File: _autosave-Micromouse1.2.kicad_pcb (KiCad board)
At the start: 2 copper layers, 70.4 x 87.9 mm, 117 parts, among them J1 USB_B, P1 CONN_01X4, Q1 Q_NMOS_DGS, Q2 Q_NMOS_DGS, Q3 Q_NMOS_DGS, Q4 Q_NMOS_DGS, Q5 Q_NMOS_DGS, Q6 Q_NMOS_DGS, U1 BAT54C, U10 CONN_02X03, U14 ferrite, U15 LMZ21701, U16 JST_Connector, U17 Switch_micromouse, U18 LMZ21701, U19 splitter, U2 DRV8833, U20 TPD3S014, U21 MKL02Z32VFG4, U22 LP38691, U23 MK66FX1M0, U24 Test_Point, U25 Test_Point, U26 Test_Point, U27 Test_Point, U28 Test_Point, U29 Test_Point, U3 ferrite, U30 Test_Point, U31 MPU-6500, U32 Motor_mount, U5 ferrite, U6 BAT54C, U9 CONN_02X03, Y1 Crystal_16MHz, Y2 32.768MHz

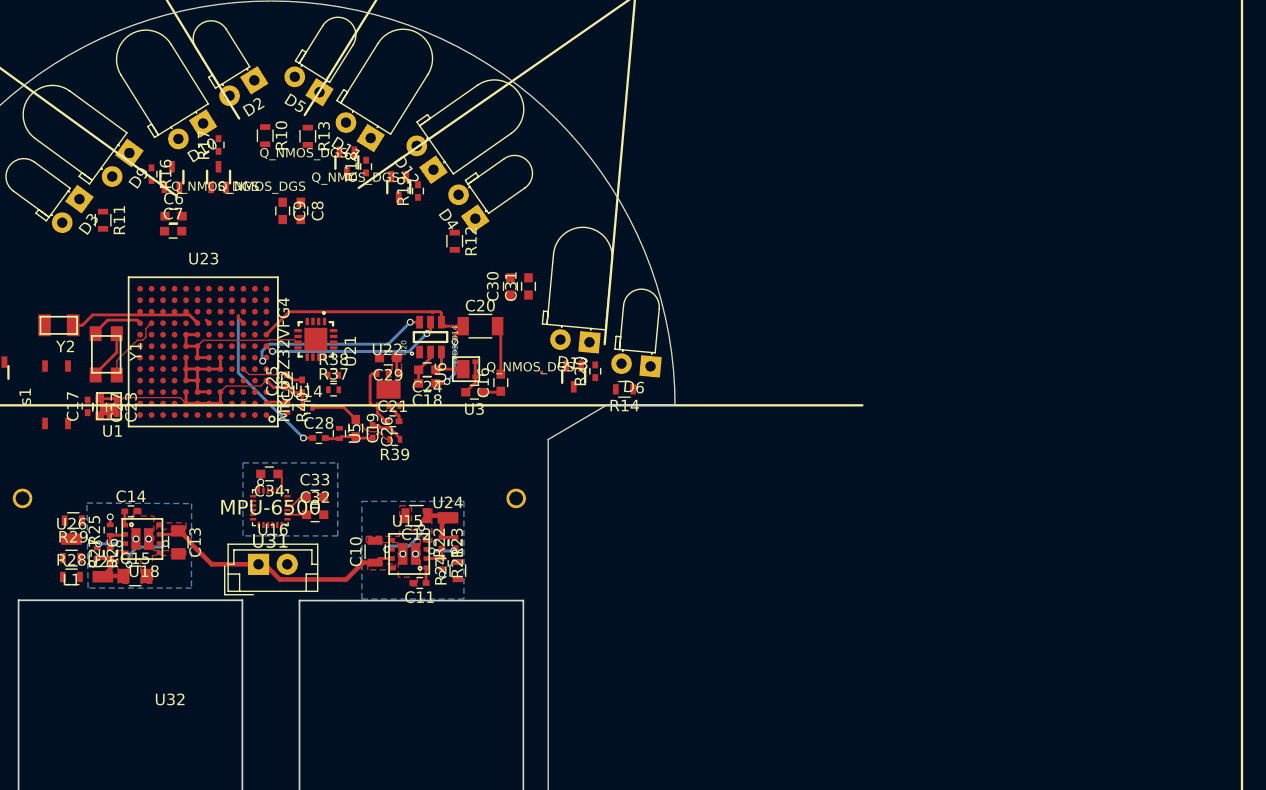
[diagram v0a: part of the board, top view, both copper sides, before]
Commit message: Change of direction
- I am changing my MCU from mk66fx1m0vmd18 to mk20dx256vlh7 as the QFN  package pcb layout is too expensive to manufacture and the  144 LQFP is takes too much real estate
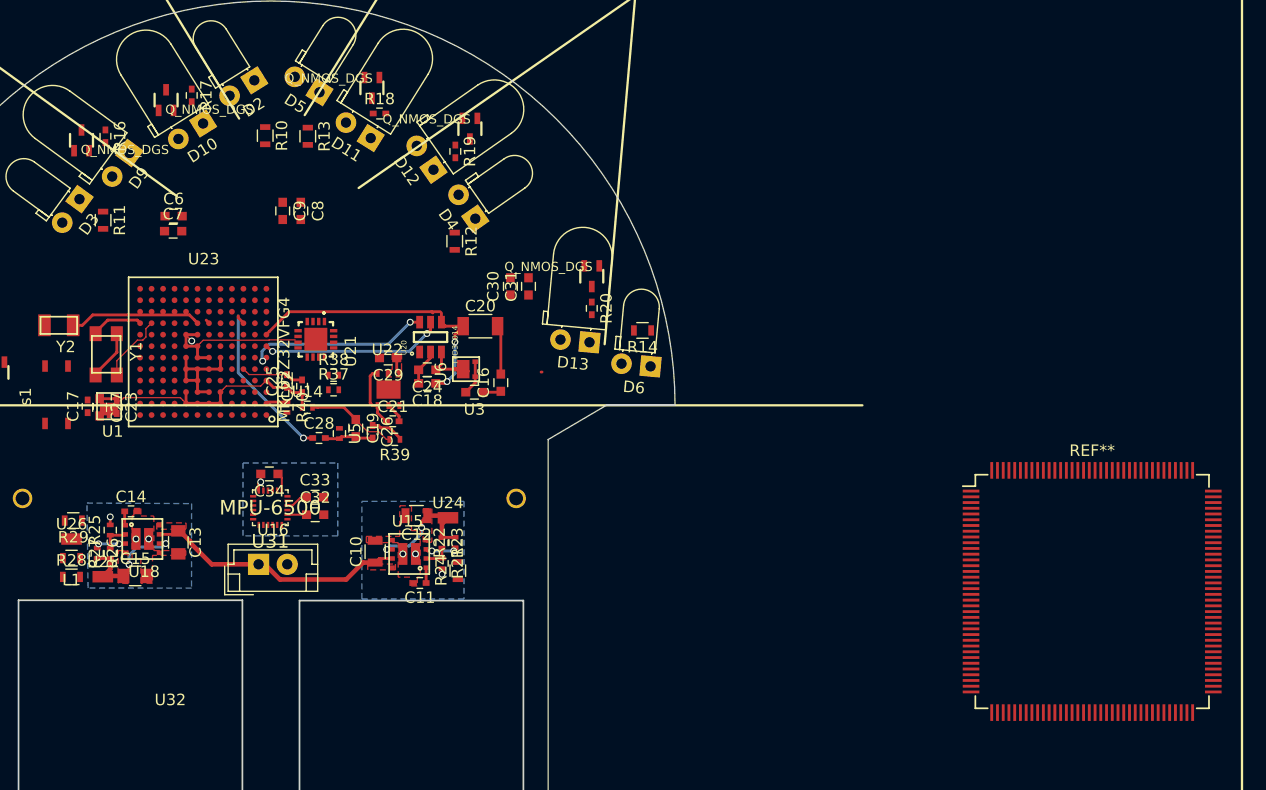
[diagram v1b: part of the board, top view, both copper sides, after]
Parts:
- added REF**: TQFP-144_20x20mm_Pitch0.5mm, Housings_QFP:TQFP-144_20x20mm_Pitch0.5mm, F.Cu at (190.3, 78.0)
- moved Q6 8.88 mm to (146.7, 50.5)
- moved Q2 8.50 mm to (102.3, 38.7)
- moved Q3 8.12 mm to (109.6, 35.2)
- moved Q5 8.01 mm to (136.1, 37.7)
- moved Q4 6.86 mm to (127.6, 34.1)
- moved R20 5.49 mm to (146.7, 53.3), turned to 270 degrees
- moved R14 5.37 mm to (151.1, 55.2)
- moved R16 5.20 mm to (104.3, 38.3)
- moved R17 4.91 mm to (111.9, 34.8), turned to 270 degrees
- moved R18 4.77 mm to (128.2, 36.3), turned to 0 degrees
- moved R19 4.74 mm to (134.8, 39.6), turned to 270 degrees
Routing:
- net (no net): track 1.04 -> 2.84 mm
- net Net-(C22-Pad1): track 34.6 -> 33.1 mm
- net GNDD: track 35.2 -> 35.9 mm, vias 5 -> 6
